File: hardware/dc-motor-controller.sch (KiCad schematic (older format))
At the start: 26 parts, among them IC1 ATMEGA88PA-P, M1 DC_motor, M2 DC_motor, M3 DC_motor, P1 Power connector, P2 ISP interface, SW1 SW_PUSH, SW2 SW_PUSH, SW3 SW_PUSH, SW4 SW_PUSH, SW5 SW_PUSH, SW6 SW_PUSH, U1 7805, U2 BA6956AN, U3 BA6956AN, U4 BA6956AN

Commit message: Some changes after reviewing the printed circuit board
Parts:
- M1, M2, M3: footprint Oturpe footprints:Big_green_chocolade_1x2 -> Oturpe footprints:Big_green_chocolate_1x2; symbol DC_motor -> DC_motor-RESCUE-dc-motor-controller
- P1: footprint Socket_Strips:Socket_Strip_Straight_1x02 -> Oturpe footprints:Small_green_chocolade_1x2
- P2: footprint Pin_Headers:Pin_Header_Straight_2x03 -> Oturpe footprints:Borg_hedged_2x03
- R1: footprint Resistors_ThroughHole:Resistor_Vertical_RM5mm -> Resistors_ThroughHole:Resistor_Horizontal_RM10mm
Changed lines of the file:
@@
 EESchema Schematic File Version 2
+LIBS:dc-motor-controller-rescue
 LIBS:power
 LIBS:device
@@
 $EndComp
 $Comp
-L DC_motor M1
+L DC_motor-RESCUE-dc-motor-controller M1
 U 1 1 5739C18C
 P 7650 1150
 F 0 "M1" H 7650 1400 60  0000 C CNN
 F 1 "DC_motor" H 7650 1550 60  0001 C CNN
-F 2 "Oturpe footprints:Big_green_chocolade_1x2" H 7650 1400 60  0001 C CNN
+F 2 "Oturpe footprints:Big_green_chocolate_1x2" H 7650 1400 60  0001 C CNN
 F 3 "" H 7650 1400 60  0000 C CNN
 	1    7650 1150
@@
 $EndComp
 $Comp
-L DC_motor M2
+L DC_motor-RESCUE-dc-motor-controller M2
 U 1 1 5739CBCB
 P 7650 3350
 F 0 "M2" H 7650 3600 60  0000 C CNN
 F 1 "DC_motor" H 7650 3750 60  0001 C CNN
-F 2 "Oturpe footprints:Big_green_chocolade_1x2" H 7650 3600 60  0001 C CNN
+F 2 "Oturpe footprints:Big_green_chocolate_1x2" H 7650 3600 60  0001 C CNN
 F 3 "" H 7650 3600 60  0000 C CNN
 	1    7650 3350
@@
 $EndComp
 $Comp
-L DC_motor M3
+L DC_motor-RESCUE-dc-motor-controller M3
 U 1 1 5739CE17
 P 7650 5450
 F 0 "M3" H 7650 5700 60  0000 C CNN
 F 1 "DC_motor" H 7650 5850 60  0001 C CNN
-F 2 "Oturpe footprints:Big_green_chocolade_1x2" H 7650 5700 60  0001 C CNN
+F 2 "Oturpe footprints:Big_green_chocolate_1x2" H 7650 5700 60  0001 C CNN
 F 3 "" H 7650 5700 60  0000 C CNN
 	1    7650 5450
@@
 F 0 "R1" V 3430 2900 50  0000 C CNN
 F 1 "1 k" V 3350 2900 50  0000 C CNN
-F 2 "Resistors_ThroughHole:Resistor_Vertical_RM5mm" V 3280 2900 50  0001 C CNN
+F 2 "Resistors_ThroughHole:Resistor_Horizontal_RM10mm" V 3280 2900 50  0001 C CNN
 F 3 "" H 3350 2900 50  0000 C CNN
 	1    3350 2900
@@
 F 0 "P1" H 1950 1750 50  0000 C CNN
 F 1 "Power connector" V 2050 1600 50  0000 C CNN
-F 2 "Socket_Strips:Socket_Strip_Straight_1x02" H 1950 1600 50  0001 C CNN
+F 2 "Oturpe footprints:Small_green_chocolade_1x2" H 1950 1600 50  0001 C CNN
 F 3 "" H 1950 1600 50  0000 C CNN
 	1    1950 1600
@@
 F 0 "P2" H 4450 4500 50  0000 C CNN
 F 1 "ISP interface" H 4450 4100 50  0000 C CNN
-F 2 "Pin_Headers:Pin_Header_Straight_2x03" H 4450 3100 50  0001 C CNN
+F 2 "Oturpe footprints:Borg_hedged_2x03" H 4450 3100 50  0001 C CNN
 F 3 "" H 4450 3100 50  0000 C CNN
 	1    4450 4300

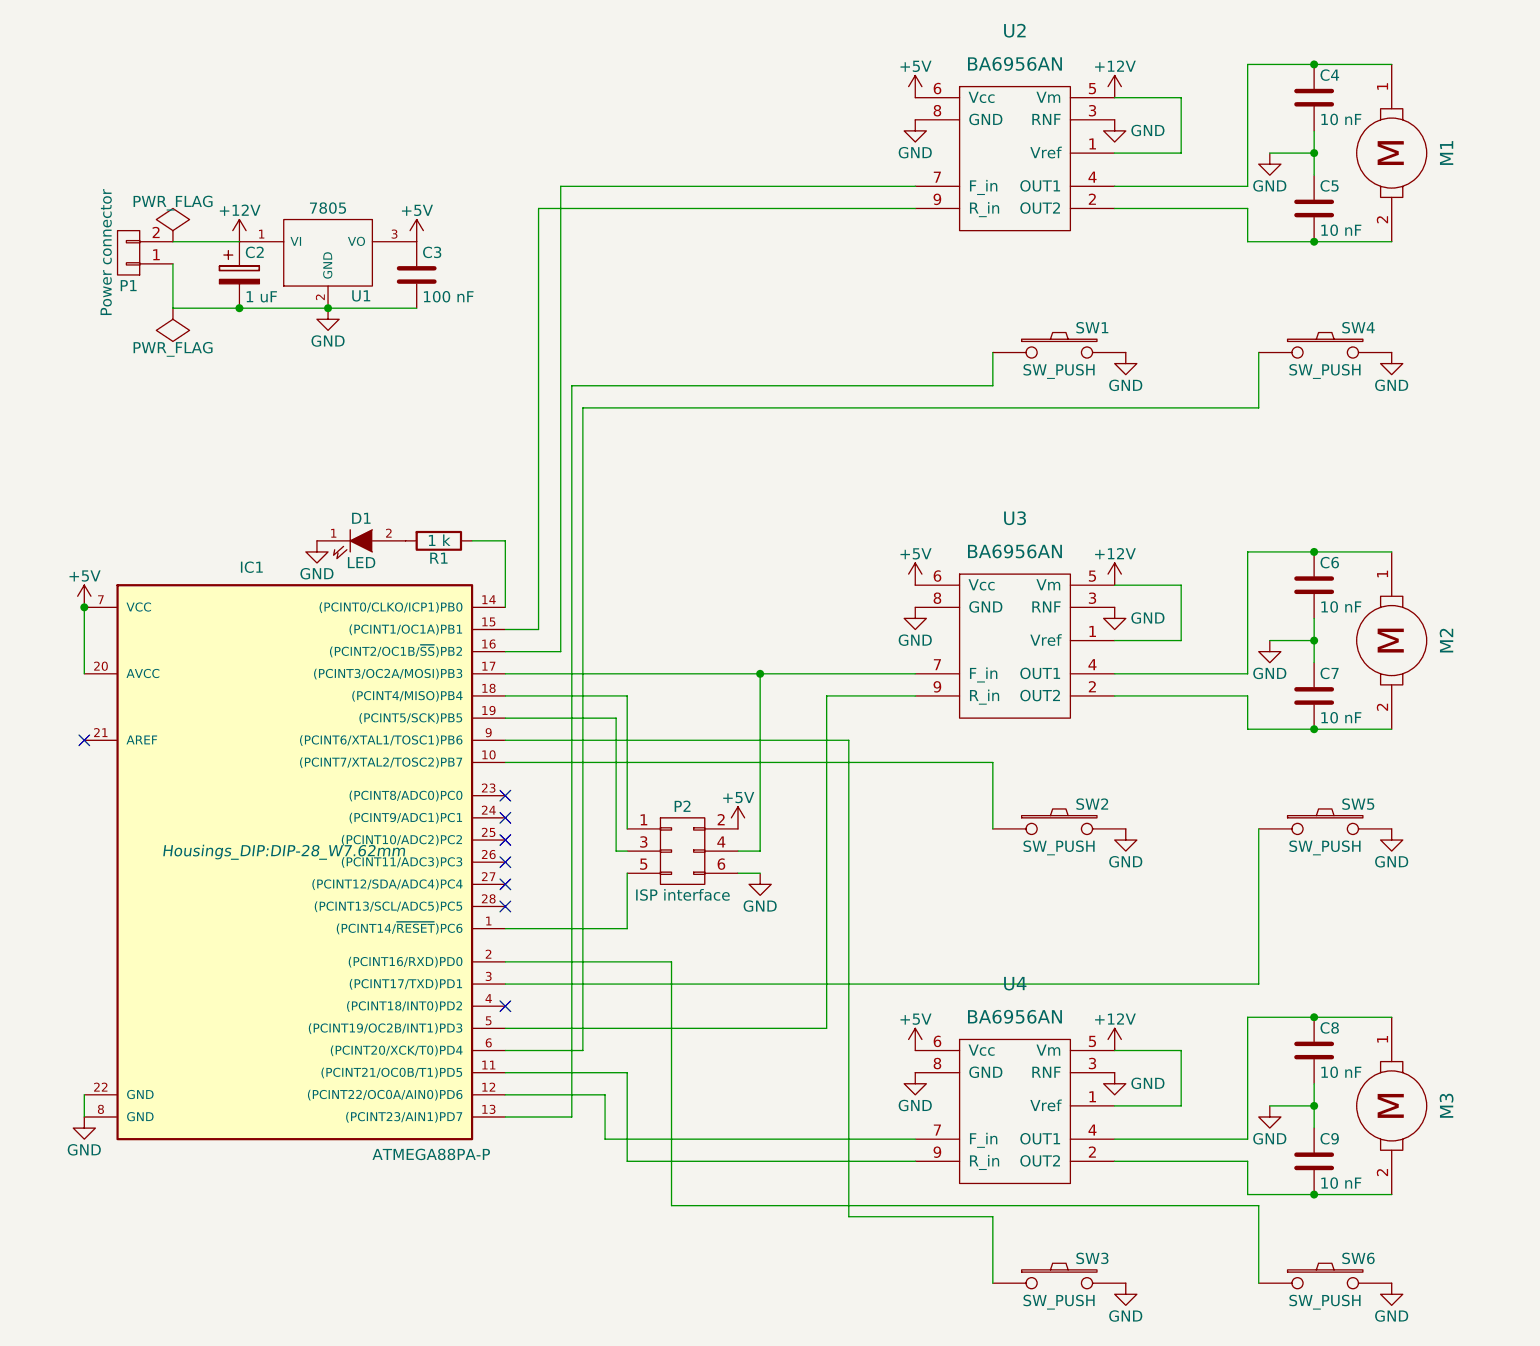
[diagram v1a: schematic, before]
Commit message: Improved part numbering of schematic
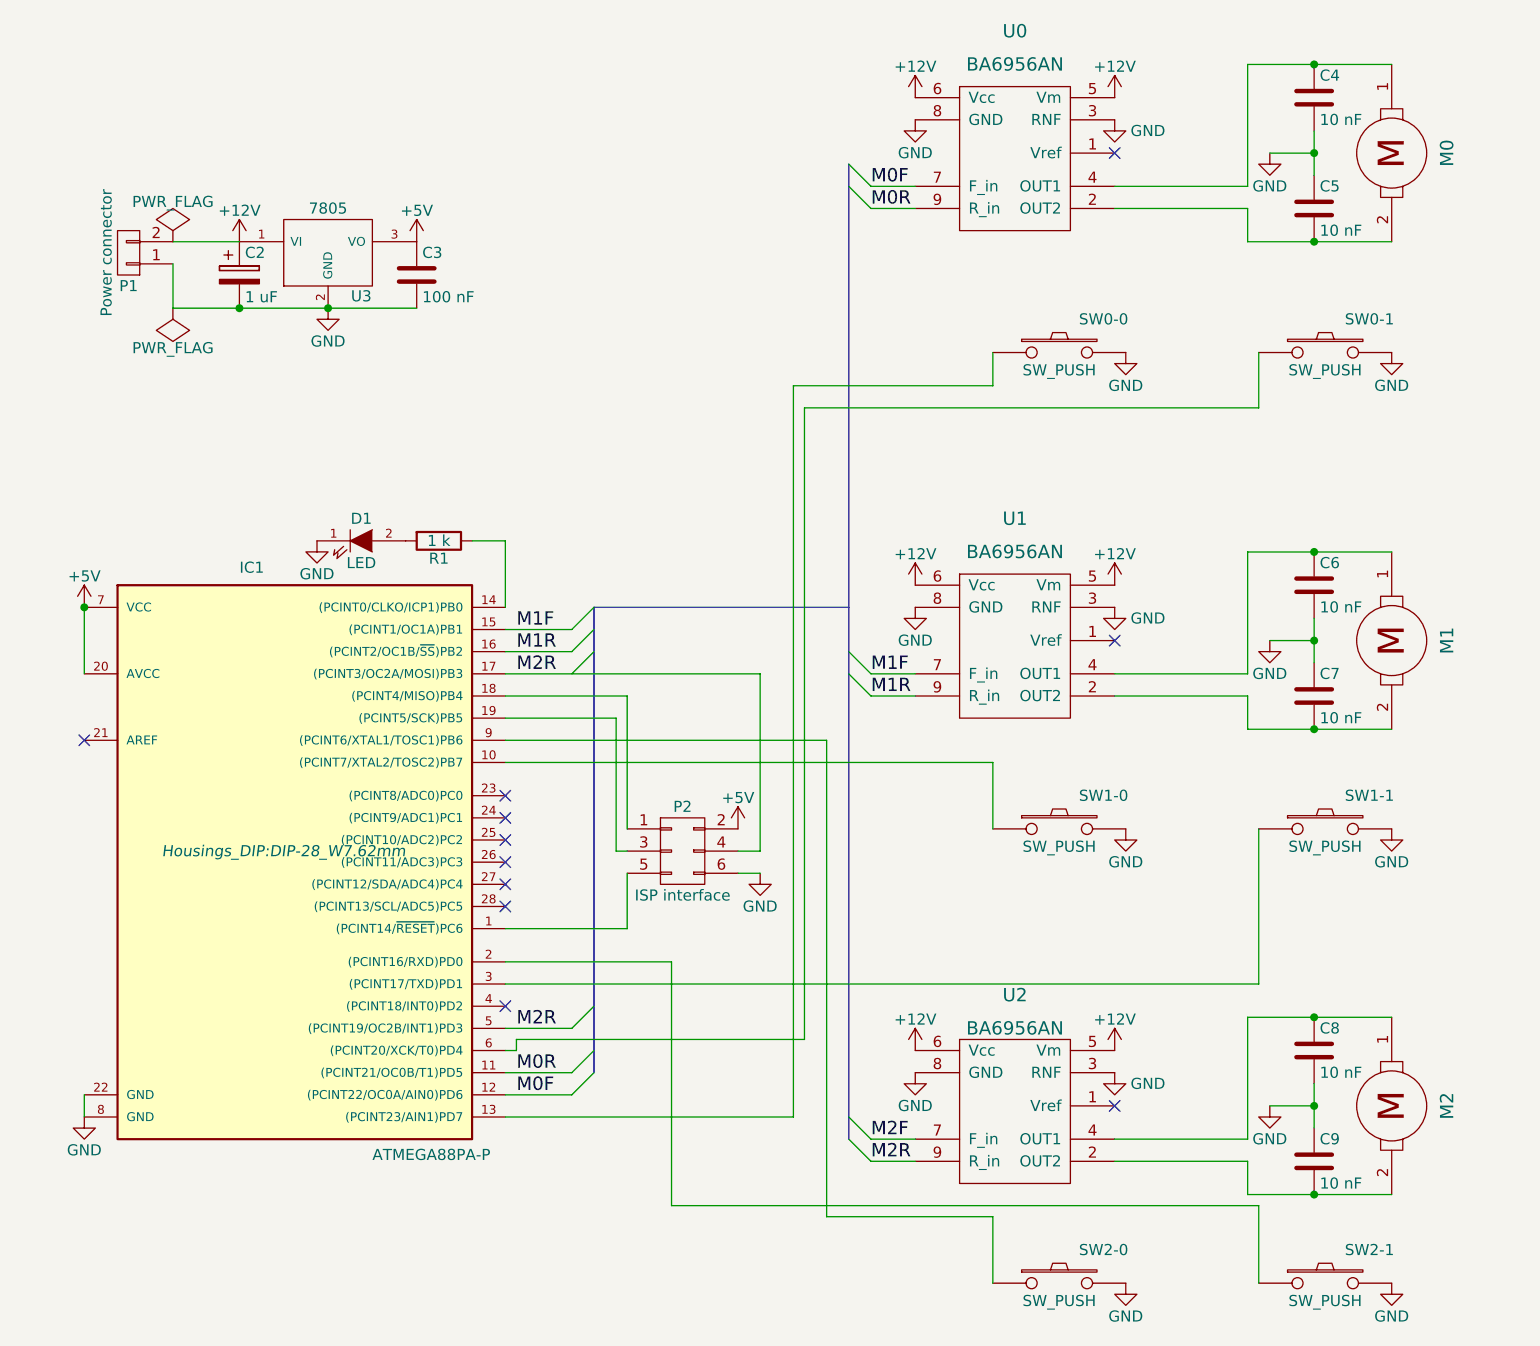
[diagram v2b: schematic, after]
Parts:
- renumbered M1 to M0, M2 to M1, M3 to M2, SW1 to SW0-0, SW4 to SW0-1, SW2 to SW1-0, SW5 to SW1-1, SW3 to SW2-0, SW6 to SW2-1, U2 to U0, U3 to U1, U4 to U2, U1 to U3
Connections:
- net +12V: now also U0.6 (Vcc), U1.6 (Vcc), U2.6 (Vcc); no longer U0.1 (Vref), U1.1 (Vref), U2.1 (Vref)
- net +5V: no longer U0.6 (Vcc), U1.6 (Vcc), U2.6 (Vcc)
- net M0F: now reaches U0.7 (F_in)
- net M0F: now also IC1.12 ((PCINT22/OC0A/AIN0)PD6); no longer IC1.16 ((PCINT2/OC1B/~SS~)PB2)
- net M0R: now reaches U0.9 (R_in)
- net M0R: now also IC1.11 ((PCINT21/OC0B/T1)PD5); no longer IC1.15 ((PCINT1/OC1A)PB1)
- net M2R: now reaches U2.9 (R_in)
- net M2R: now also IC1.17 ((PCINT3/OC2A/MOSI)PB3), IC1.5 ((PCINT19/OC2B/INT1)PD3), P2.4 (P4); no longer IC1.11 ((PCINT21/OC0B/T1)PD5)
- net M2F: now reaches U2.7 (F_in)
- net M2F: no longer IC1.12 ((PCINT22/OC0A/AIN0)PD6)
- net M1R: now reaches U1.9 (R_in)
- net M1R: now also IC1.16 ((PCINT2/OC1B/~SS~)PB2); no longer IC1.5 ((PCINT19/OC2B/INT1)PD3)
- new net M1F: IC1.15 ((PCINT1/OC1A)PB1), U1.7 (F_in)
- no-connect marks 8 -> 11

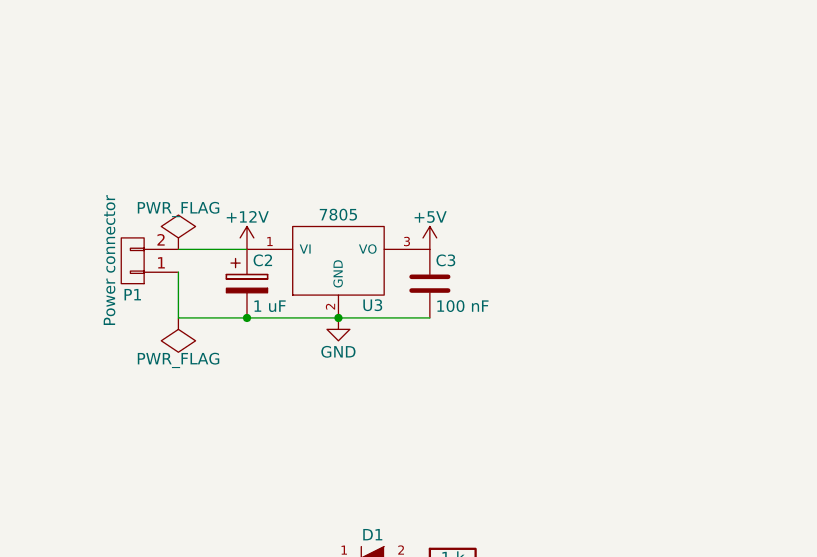
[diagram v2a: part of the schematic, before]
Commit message: Add a power switch to schemaic
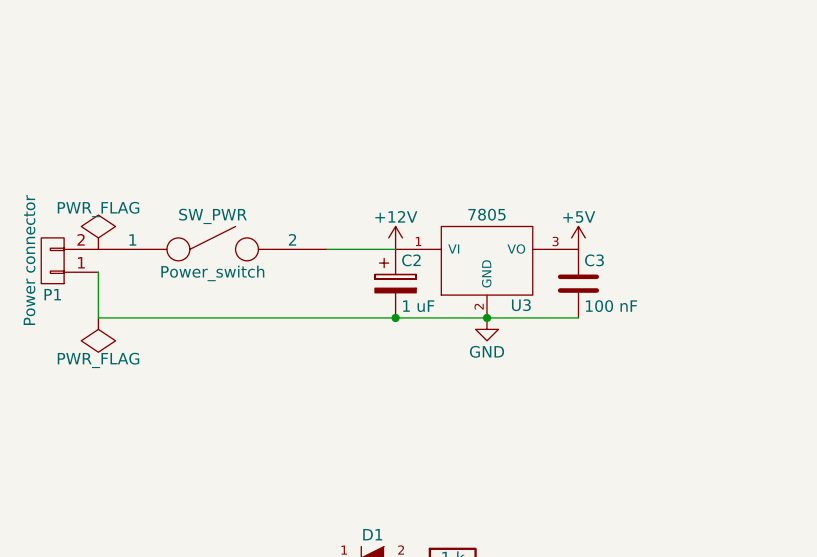
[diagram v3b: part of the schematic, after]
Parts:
- added SW_PWR: Power_switch, symbol SPST
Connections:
- net +12V: now also SW_PWR.2; no longer P1.2 (P2)
- new net: P1.2 (P2), SW_PWR.1
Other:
- moved on the sheet: C2, C3, P1, U3
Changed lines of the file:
@@
 L GND #PWR021
 U 1 1 573C3CB2
-P 2850 1850
-F 0 "#PWR021" H 2850 1600 50  0001 C CNN
-F 1 "GND" H 2850 1700 50  0000 C CNN
-F 2 "" H 2850 1850 50  0000 C CNN
-F 3 "" H 2850 1850 50  0000 C CNN
-	1    2850 1850
+P 3500 1850
+F 0 "#PWR021" H 3500 1600 50  0001 C CNN
+F 1 "GND" H 3500 1700 50  0000 C CNN
+F 2 "" H 3500 1850 50  0000 C CNN
+F 3 "" H 3500 1850 50  0000 C CNN
+	1    3500 1850
 	1    0    0    -1
 $EndComp
@@
 L +12V #PWR022
 U 1 1 573C3D00
-P 2450 1550
-F 0 "#PWR022" H 2450 1400 50  0001 C CNN
-F 1 "+12V" H 2450 1690 50  0000 C CNN
-F 2 "" H 2450 1550 50  0000 C CNN
-F 3 "" H 2450 1550 50  0000 C CNN
-	1    2450 1550
+P 3100 1550
+F 0 "#PWR022" H 3100 1400 50  0001 C CNN
+F 1 "+12V" H 3100 1690 50  0000 C CNN
+F 2 "" H 3100 1550 50  0000 C CNN
+F 3 "" H 3100 1550 50  0000 C CNN
+	1    3100 1550
 	1    0    0    -1
 $EndComp
@@
 L +5V #PWR023
 U 1 1 573C3D4E
-P 3250 1550
-F 0 "#PWR023" H 3250 1400 50  0001 C CNN
-F 1 "+5V" H 3250 1690 50  0000 C CNN
-F 2 "" H 3250 1550 50  0000 C CNN
-F 3 "" H 3250 1550 50  0000 C CNN
-	1    3250 1550
+P 3900 1550
+F 0 "#PWR023" H 3900 1400 50  0001 C CNN
+F 1 "+5V" H 3900 1690 50  0000 C CNN
+F 2 "" H 3900 1550 50  0000 C CNN
+F 3 "" H 3900 1550 50  0000 C CNN
+	1    3900 1550
 	1    0    0    -1
 $EndComp
@@
 L C C3
 U 1 1 573C3D9C
-P 3250 1700
-F 0 "C3" H 3275 1800 50  0000 L CNN
-F 1 "100 nF" H 3275 1600 50  0000 L CNN
-F 2 "Capacitors_ThroughHole:C_Rect_L7_W2.5_P5" H 3288 1550 50  0001 C CNN
-F 3 "" H 3250 1700 50  0000 C CNN
-	1    3250 1700
+P 3900 1700
+F 0 "C3" H 3925 1800 50  0000 L CNN
+F 1 "100 nF" H 3925 1600 50  0000 L CNN
+F 2 "Capacitors_ThroughHole:C_Rect_L7_W2.5_P5" H 3938 1550 50  0001 C CNN
+F 3 "" H 3900 1700 50  0000 C CNN
+	1    3900 1700
 	1    0    0    -1
 $EndComp
@@
 L CP C2
 U 1 1 573C3E13
-P 2450 1700
-F 0 "C2" H 2475 1800 50  0000 L CNN
-F 1 "1 uF" H 2475 1600 50  0000 L CNN
-F 2 "Capacitors_ThroughHole:C_Radial_D5_L6_P2.5" H 2488 1550 50  0001 C CNN
-F 3 "" H 2450 1700 50  0000 C CNN
-	1    2450 1700
+P 3100 1700
+F 0 "C2" H 3125 1800 50  0000 L CNN
+F 1 "1 uF" H 3125 1600 50  0000 L CNN
+F 2 "Capacitors_ThroughHole:C_Radial_D5_L6_P2.5" H 3138 1550 50  0001 C CNN
+F 3 "" H 3100 1700 50  0000 C CNN
+	1    3100 1700
 	1    0    0    -1
 $EndComp
@@
 L CONN_01X02 P1
 U 1 1 57404E3E
-P 1950 1600
-F 0 "P1" H 1950 1750 50  0000 C CNN
-F 1 "Power connector" V 2050 1600 50  0000 C CNN
-F 2 "Oturpe footprints:Small_green_chocolade_1x2" H 1950 1600 50  0001 C CNN
-F 3 "" H 1950 1600 50  0000 C CNN
-	1    1950 1600
+P 1600 1600
+F 0 "P1" H 1600 1750 50  0000 C CNN
+F 1 "Power connector" V 1700 1600 50  0000 C CNN
+F 2 "Oturpe footprints:Small_green_chocolade_1x2" H 1600 1600 50  0001 C CNN
+F 3 "" H 1600 1600 50  0000 C CNN
+	1    1600 1600
 	-1   0    0    1
 $EndComp
@@
 L PWR_FLAG #FLG027
 U 1 1 57427172
-P 2150 1550
-F 0 "#FLG027" H 2150 1645 50  0001 C CNN
-F 1 "PWR_FLAG" H 2150 1730 50  0000 C CNN
-F 2 "" H 2150 1550 50  0000 C CNN
-F 3 "" H 2150 1550 50  0000 C CNN
-	1    2150 1550
+P 1800 1550
+F 0 "#FLG027" H 1800 1645 50  0001 C CNN
+F 1 "PWR_FLAG" H 1800 1730 50  0000 C CNN
+F 2 "" H 1800 1550 50  0000 C CNN
+F 3 "" H 1800 1550 50  0000 C CNN
+	1    1800 1550
 	1    0    0    -1
 $EndComp
@@
 L PWR_FLAG #FLG028
 U 1 1 574325F0
-P 2150 1850
-F 0 "#FLG028" H 2150 1945 50  0001 C CNN
-F 1 "PWR_FLAG" H 2150 2030 50  0000 C CNN
-F 2 "" H 2150 1850 50  0000 C CNN
-F 3 "" H 2150 1850 50  0000 C CNN
-	1    2150 1850
+P 1800 1850
+F 0 "#FLG028" H 1800 1945 50  0001 C CNN
+F 1 "PWR_FLAG" H 1800 2030 50  0000 C CNN
+F 2 "" H 1800 1850 50  0000 C CNN
+F 3 "" H 1800 1850 50  0000 C CNN
+	1    1800 1850
 	-1   0    0    1
 $EndComp
@@
 L 7805_oturpe U3
 U 1 1 574C5798
-P 2850 1600
-F 0 "U3" H 3000 1404 50  0000 C CNN
-F 1 "7805" H 2850 1800 50  0000 C CNN
-F 2 "TO_SOT_Packages_THT:TO-220_Neutral123_Vertical" H 2850 1600 50  0001 C CNN
-F 3 "" H 2850 1600 50  0000 C CNN
-	1    2850 1600
+P 3500 1600
+F 0 "U3" H 3650 1404 50  0000 C CNN
+F 1 "7805" H 3500 1800 50  0000 C CNN
+F 2 "TO_SOT_Packages_THT:TO-220_Neutral123_Vertical" H 3500 1600 50  0001 C CNN
+F 3 "" H 3500 1600 50  0000 C CNN
+	1    3500 1600
 	1    0    0    -1
 $EndComp
@@
 	5850 5950 5850 6250
 Wire Wire Line
-	2150 1850 3250 1850
-Connection ~ 2850 1850
-Wire Wire Line
-	2450 1550 2150 1550
-Wire Wire Line
-	2150 1850 2150 1650
-Connection ~ 2450 1850
+	1800 1850 3900 1850
+Connection ~ 3500 1850
+Wire Wire Line
+	3100 1550 2800 1550
+Wire Wire Line
+	1800 1850 1800 1650
+Connection ~ 3100 1850
 Wire Wire Line
 	3650 4650 4200 4650
@@
 Text Label 3700 3500 0    60   ~ 0
 M2R
+$Comp
+L SPST SW_PWR
+U 1 1 576A4F51
+P 2300 1550
+F 0 "SW_PWR" H 2300 1700 50  0000 C CNN
+F 1 "Power_switch" H 2300 1450 50  0000 C CNN
+F 2 "" H 2300 1550 50  0000 C CNN
+F 3 "" H 2300 1550 50  0000 C CNN
+	1    2300 1550
+	1    0    0    -1
+$EndComp
 $EndSCHEMATC

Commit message: Update schematic annotation
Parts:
- renumbered SW_PWR to SW_PWR1
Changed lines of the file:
@@
 M2R
 $Comp
-L SPST SW_PWR
+L SPST SW_PWR1
 U 1 1 576A4F51
 P 2300 1550
-F 0 "SW_PWR" H 2300 1700 50  0000 C CNN
+F 0 "SW_PWR1" H 2300 1700 50  0000 C CNN
 F 1 "Power_switch" H 2300 1450 50  0000 C CNN
 F 2 "" H 2300 1550 50  0000 C CNN
